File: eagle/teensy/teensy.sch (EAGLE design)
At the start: 5 parts

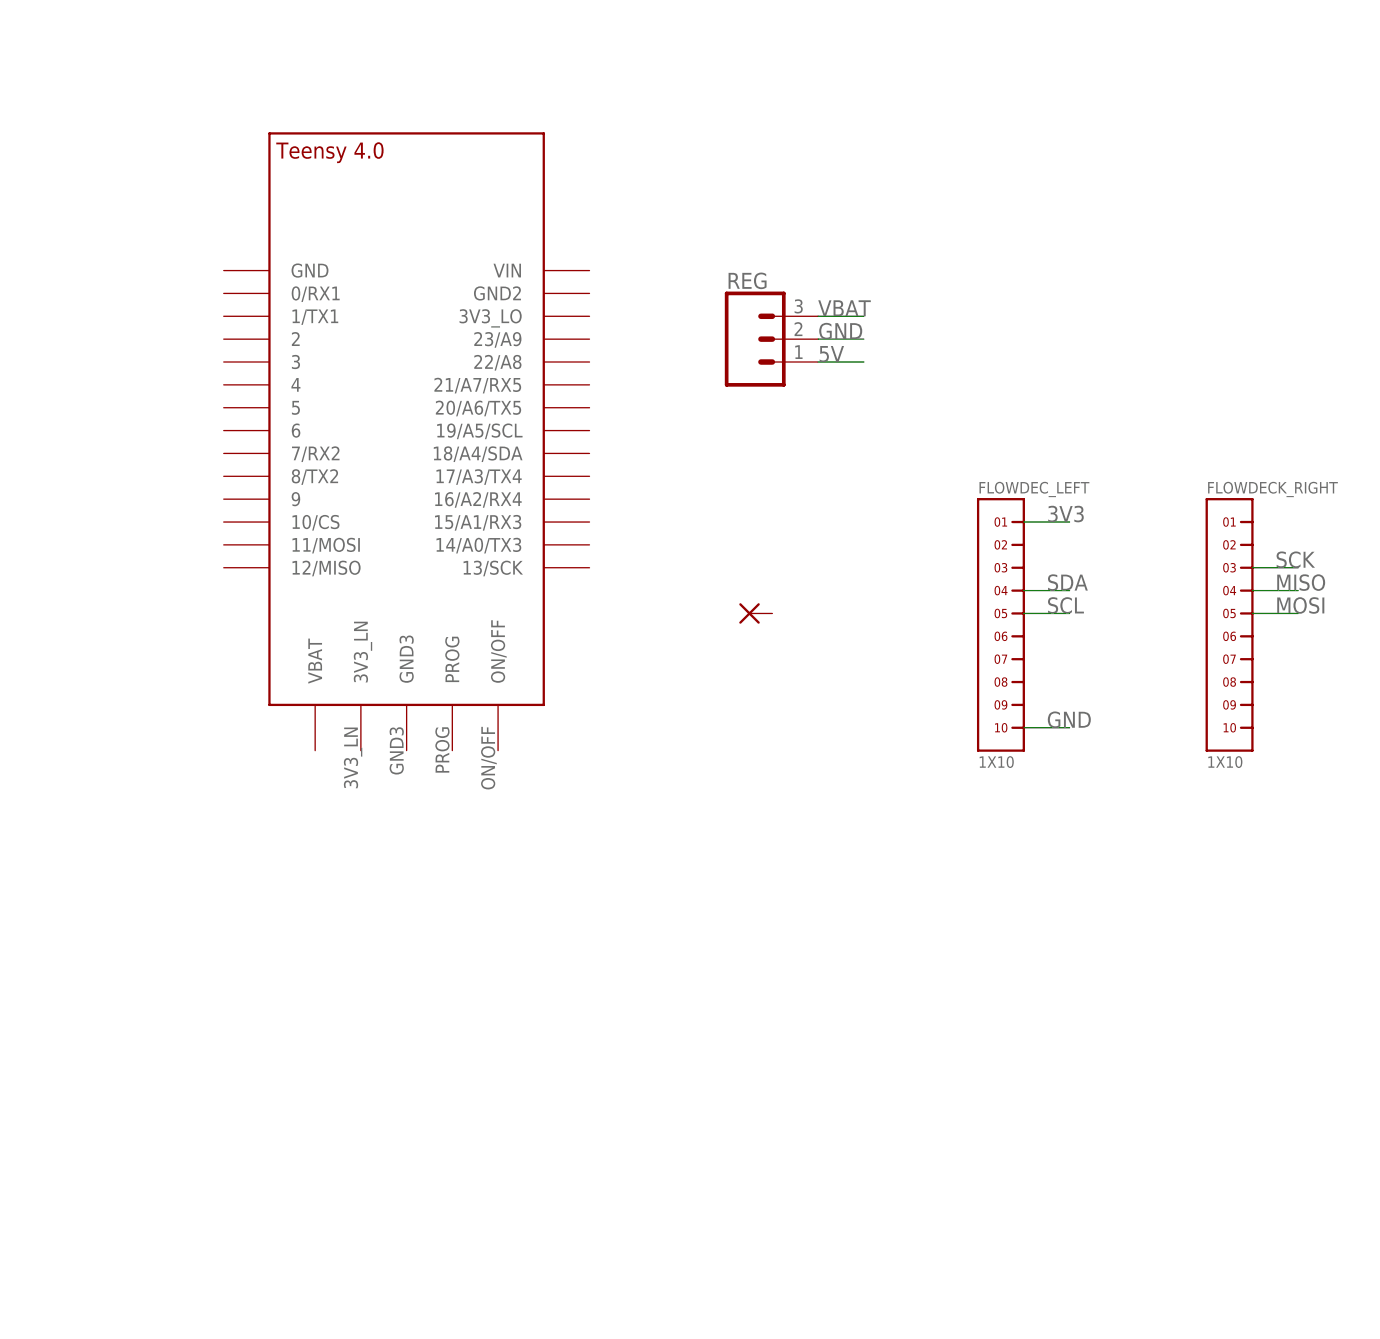
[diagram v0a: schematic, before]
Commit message: renamed:    eagle/teensy/core.sch -> eagle/teensy/teensy.sch
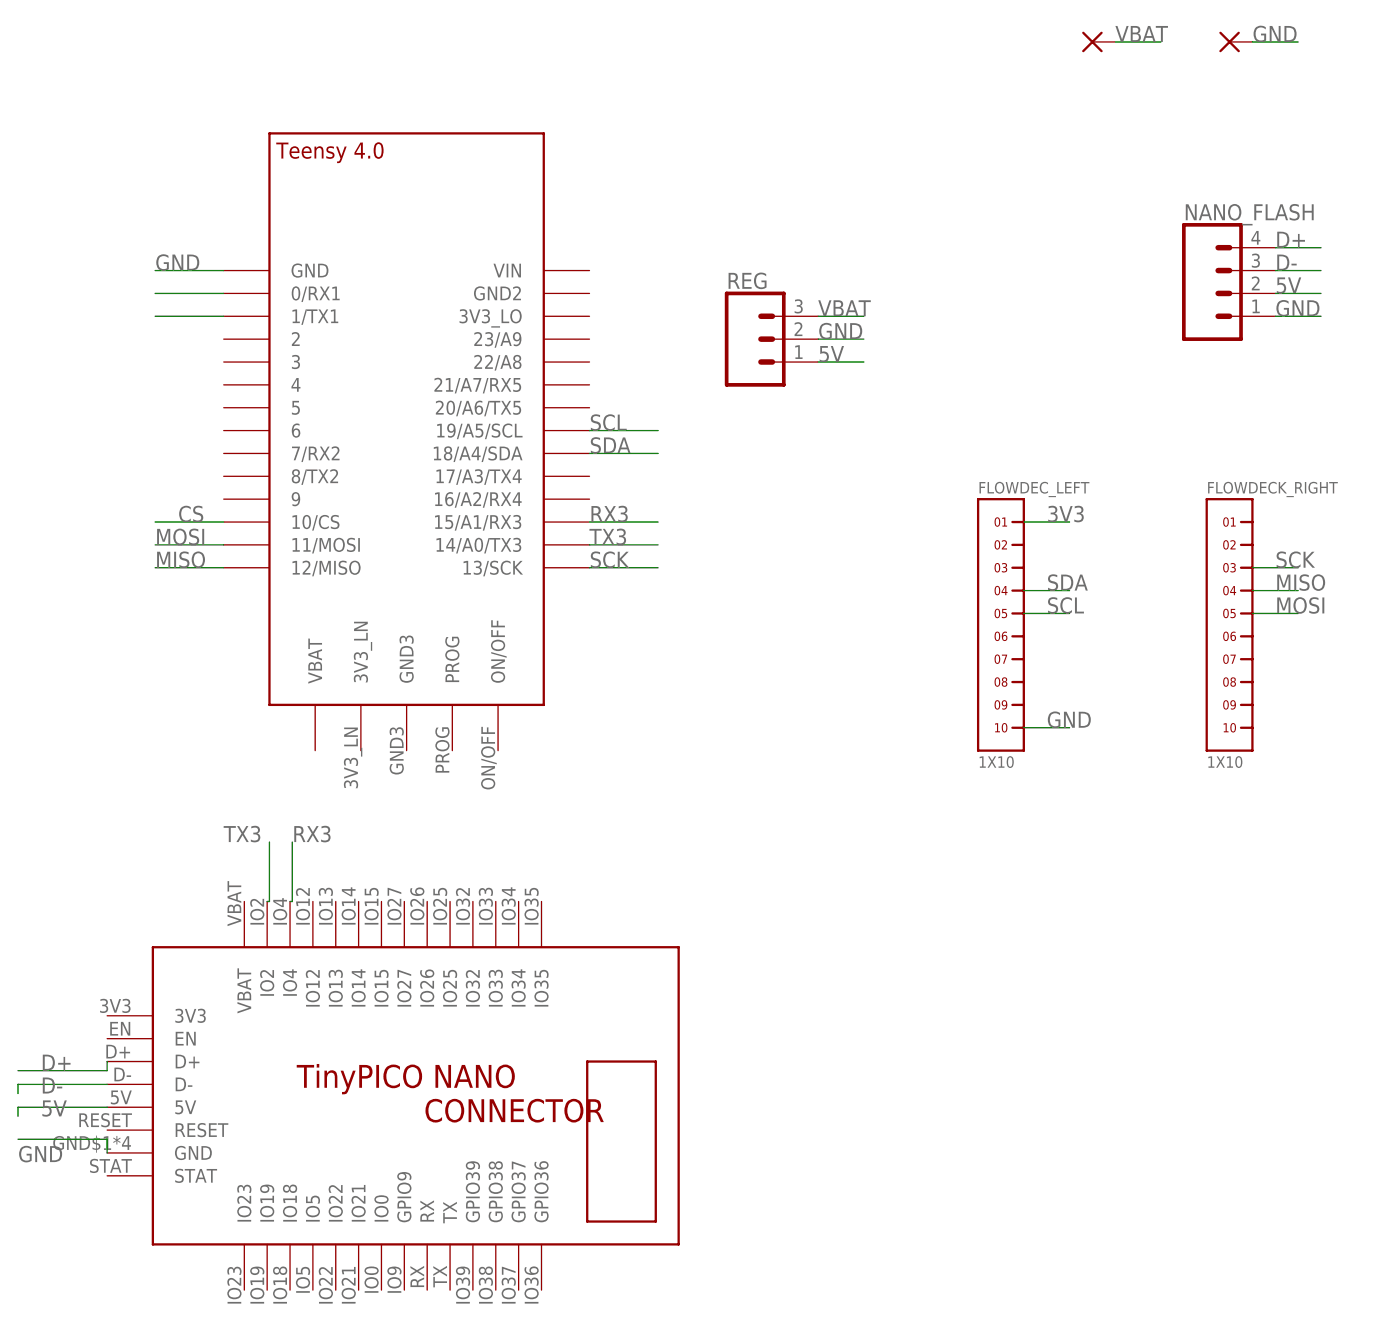
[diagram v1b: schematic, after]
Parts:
- removed PAD18: (no value), wirepad:SMD2
- added GND, VBAT: (no value), wirepad:SMD5
- added NANO_FLASH: (no value), SparkFun-Connectors:CONN_041X04_NO_SILK
- added U$2: TINYPICO-NANO-CONNECTOR, TinyPICO_NANO_Eagle:TINYPICO-NANO-CONNECTOR
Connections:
- new net CS: U$1.10/CS
- new net D+: NANO_FLASH.4, U$2.D+
- new net D-: NANO_FLASH.3, U$2.D-
- new net N$8: U$1.0/RX1
- new net N$9: U$1.1/TX1
- new net RX3: U$1.15/A1/RX3, U$2.IO4
- new net TX3: U$1.14/A0/TX3, U$2.IO2
- net 5V: now also NANO_FLASH.2, U$2.5V
- net GND: now also GND.P, NANO_FLASH.1, U$1.GND, U$2.GND
- net MISO: now also U$1.12/MISO
- net MOSI: now also U$1.11/MOSI
- net SCK: now also U$1.13/SCK
- net SCL: now also U$1.19/A5/SCL
- net SDA: now also U$1.18/A4/SDA
- net VBAT: now also VBAT.P
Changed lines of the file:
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@@
 <?xml version="1.0" encoding="utf-8"?>
 <!DOCTYPE eagle SYSTEM "eagle.dtd">
-<eagle version="9.6.2">
+<eagle version="9.1.1">
 <drawing>
 <settings>
@@
 <parts>
 <part name="REG" library="SparkFun-Connectors" deviceset="CONN_03" device="1X03_NO_SILK"/>
-<part name="PAD18" library="wirepad" deviceset="SMD2" device=""/>
 <part name="U$1" library="TEENSY 4.0" deviceset="TEENSY_4.0" device=""/>
 <part name="FLOWDEC_LEFT" library="headers(2mm)" deviceset="1X10" device=""/>
 <part name="FLOWDECK_RIGHT" library="headers(2mm)" deviceset="1X10" device=""/>
+<part name="U$2" library="TinyPICO_NANO_Eagle" deviceset="TINYPICO-NANO-CONNECTOR" device=""/>
+<part name="VBAT" library="wirepad" deviceset="SMD5" device=""/>
+<part name="GND" library="wirepad" deviceset="SMD5" device=""/>
+<part name="NANO_FLASH" library="SparkFun-Connectors" deviceset="CONN_04" device="1X04_NO_SILK"/>
 </parts>
 <sheets>
@@
 <attribute name="NAME" x="50.8" y="114.808" size="1.778" layer="95" font="vector"/>
 </instance>
-<instance part="PAD18" gate="1" x="53.34" y="78.74" smashed="yes">
-<attribute name="VALUE" x="52.197" y="75.438" size="1.778" layer="96"/>
-</instance>
 <instance part="U$1" gate="G$1" x="15.24" y="104.14" smashed="yes"/>
 <instance part="FLOWDEC_LEFT" gate="G$1" x="81.28" y="76.2" smashed="yes">
@@
 <attribute name="VALUE" x="104.14" y="61.595" size="1.27" layer="96" font="vector"/>
 </instance>
+<instance part="U$2" gate="G$1" x="15.24" y="25.4"/>
+<instance part="VBAT" gate="1" x="91.44" y="142.24" smashed="yes">
+<attribute name="VALUE" x="90.297" y="138.938" size="1.778" layer="96"/>
+</instance>
+<instance part="GND" gate="1" x="106.68" y="142.24" smashed="yes">
+<attribute name="VALUE" x="105.537" y="138.938" size="1.778" layer="96"/>
+</instance>
+<instance part="NANO_FLASH" gate="J1" x="106.68" y="114.3"/>
 </instances>
 <busses>
@@
 <label x="86.36" y="66.04" size="1.778" layer="95"/>
 </segment>
+<segment>
+<pinref part="GND" gate="1" pin="P"/>
+<wire x1="109.22" y1="142.24" x2="114.3" y2="142.24" width="0.1524" layer="91"/>
+<label x="109.22" y="142.24" size="1.778" layer="95"/>
+</segment>
+<segment>
+<pinref part="U$2" gate="G$1" pin="GND"/>
+<wire x1="-18.034" y1="18.796" x2="-18.034" y2="20.32" width="0.1524" layer="91"/>
+<wire x1="-18.034" y1="20.32" x2="-27.94" y2="20.32" width="0.1524" layer="91"/>
+<label x="-27.94" y="17.78" size="1.778" layer="95"/>
+</segment>
+<segment>
+<pinref part="U$1" gate="G$1" pin="GND"/>
+<wire x1="-5.08" y1="116.84" x2="-12.7" y2="116.84" width="0.1524" layer="91"/>
+<label x="-12.7" y="116.84" size="1.778" layer="95"/>
+</segment>
+<segment>
+<pinref part="NANO_FLASH" gate="J1" pin="1"/>
+<wire x1="111.76" y1="111.76" x2="116.84" y2="111.76" width="0.1524" layer="91"/>
+<label x="111.76" y="111.76" size="1.778" layer="95"/>
+</segment>
 </net>
 <net name="5V" class="0">
@@
 <label x="60.96" y="106.68" size="1.778" layer="95"/>
 </segment>
+<segment>
+<pinref part="U$2" gate="G$1" pin="5V"/>
+<wire x1="-18.034" y1="23.876" x2="-27.94" y2="23.876" width="0.1524" layer="91"/>
+<wire x1="-27.94" y1="23.876" x2="-27.94" y2="22.86" width="0.1524" layer="91"/>
+<label x="-25.4" y="22.86" size="1.778" layer="95"/>
+</segment>
+<segment>
+<pinref part="NANO_FLASH" gate="J1" pin="2"/>
+<wire x1="111.76" y1="114.3" x2="116.84" y2="114.3" width="0.1524" layer="91"/>
+<label x="111.76" y="114.3" size="1.778" layer="95"/>
+</segment>
 </net>
 <net name="VBAT" class="0">
@@
 <label x="60.96" y="111.76" size="1.778" layer="95"/>
 </segment>
+<segment>
+<pinref part="VBAT" gate="1" pin="P"/>
+<wire x1="93.98" y1="142.24" x2="99.06" y2="142.24" width="0.1524" layer="91"/>
+<label x="93.98" y="142.24" size="1.778" layer="95"/>
+</segment>
 </net>
 <net name="3V3" class="0">
@@
 <label x="86.36" y="81.28" size="1.778" layer="95"/>
 </segment>
+<segment>
+<pinref part="U$1" gate="G$1" pin="18/A4/SDA"/>
+<wire x1="35.56" y1="96.52" x2="43.18" y2="96.52" width="0.1524" layer="91"/>
+<label x="35.56" y="96.52" size="1.778" layer="95"/>
+</segment>
 </net>
 <net name="SCL" class="0">
@@
 <label x="86.36" y="78.74" size="1.778" layer="95"/>
 </segment>
+<segment>
+<pinref part="U$1" gate="G$1" pin="19/A5/SCL"/>
+<wire x1="35.56" y1="99.06" x2="43.18" y2="99.06" width="0.1524" layer="91"/>
+<label x="35.56" y="99.06" size="1.778" layer="95"/>
+</segment>
 </net>
 <net name="SCK" class="0">
@@
 <label x="111.76" y="83.82" size="1.778" layer="95"/>
 </segment>
+<segment>
+<pinref part="U$1" gate="G$1" pin="13/SCK"/>
+<wire x1="35.56" y1="83.82" x2="43.18" y2="83.82" width="0.1524" layer="91"/>
+<label x="35.56" y="83.82" size="1.778" layer="95"/>
+</segment>
 </net>
 <net name="MISO" class="0">
@@
 <label x="111.76" y="81.28" size="1.778" layer="95"/>
 </segment>
+<segment>
+<pinref part="U$1" gate="G$1" pin="12/MISO"/>
+<wire x1="-5.08" y1="83.82" x2="-12.7" y2="83.82" width="0.1524" layer="91"/>
+<label x="-12.7" y="83.82" size="1.778" layer="95"/>
+</segment>
 </net>
 <net name="MOSI" class="0">
@@
 <label x="111.76" y="78.74" size="1.778" layer="95"/>
 </segment>
-</net>
+<segment>
+<pinref part="U$1" gate="G$1" pin="11/MOSI"/>
+<wire x1="-12.7" y1="86.36" x2="-5.08" y2="86.36" width="0.1524" layer="91"/>
+<label x="-12.7" y="86.36" size="1.778" layer="95"/>
+</segment>
+</net>
+<net name="D+" class="0">
+<segment>
+<pinref part="U$2" gate="G$1" pin="D+"/>
+<wire x1="-18.034" y1="28.956" x2="-18.034" y2="27.94" width="0.1524" layer="91"/>
+<wire x1="-18.034" y1="27.94" x2="-27.94" y2="27.94" width="0.1524" layer="91"/>
+<label x="-25.4" y="27.94" size="1.778" layer="95"/>
+</segment>
+<segment>
+<pinref part="NANO_FLASH" gate="J1" pin="4"/>
+<wire x1="111.76" y1="119.38" x2="116.84" y2="119.38" width="0.1524" layer="91"/>
+<label x="111.76" y="119.38" size="1.778" layer="95"/>
+</segment>
+</net>
+<net name="D-" class="0">
+<segment>
+<pinref part="U$2" gate="G$1" pin="D-"/>
+<wire x1="-18.034" y1="26.416" x2="-27.94" y2="26.416" width="0.1524" layer="91"/>
+<wire x1="-27.94" y1="26.416" x2="-27.94" y2="25.4" width="0.1524" layer="91"/>
+<label x="-25.4" y="25.4" size="1.778" layer="95"/>
+</segment>
+<segment>
+<pinref part="NANO_FLASH" gate="J1" pin="3"/>
+<wire x1="111.76" y1="116.84" x2="116.84" y2="116.84" width="0.1524" layer="91"/>
+<label x="111.76" y="116.84" size="1.778" layer="95"/>
+</segment>
+</net>
+<net name="CS" class="0">
+<segment>
+<pinref part="U$1" gate="G$1" pin="10/CS"/>
+<wire x1="-5.08" y1="88.9" x2="-12.7" y2="88.9" width="0.1524" layer="91"/>
+<label x="-10.16" y="88.9" size="1.778" layer="95"/>
+</segment>
+</net>
+<net name="N$8" class="0">
+<segment>
+<pinref part="U$1" gate="G$1" pin="0/RX1"/>
+<wire x1="-5.08" y1="114.3" x2="-12.7" y2="114.3" width="0.1524" layer="91"/>
+</segment>
+</net>
+<net name="N$9" class="0">
+<segment>
+<pinref part="U$1" gate="G$1" pin="1/TX1"/>
+<wire x1="-5.08" y1="111.76" x2="-12.7" y2="111.76" width="0.1524" layer="91"/>
+</segment>
+</net>
+<net name="TX3" class="0">
+<segment>
+<pinref part="U$1" gate="G$1" pin="14/A0/TX3"/>
+<wire x1="35.56" y1="86.36" x2="43.18" y2="86.36" width="0.1524" layer="91"/>
+<label x="35.56" y="86.36" size="1.778" layer="95"/>
+</segment>
+<segment>
+<pinref part="U$2" gate="G$1" pin="IO2"/>
+<wire x1="-0.254" y1="46.736" x2="0" y2="46.736" width="0.1524" layer="91"/>
+<wire x1="0" y1="46.736" x2="0" y2="53.34" width="0.1524" layer="91"/>
+<label x="-5.08" y="53.34" size="1.778" layer="95"/>
+</segment>
+</net>
+<net name="RX3" class="0">
+<segment>
+<pinref part="U$1" gate="G$1" pin="15/A1/RX3"/>
+<wire x1="35.56" y1="88.9" x2="43.18" y2="88.9" width="0.1524" layer="91"/>
+<label x="35.56" y="88.9" size="1.778" layer="95"/>
+</segment>
+<segment>
+<pinref part="U$2" gate="G$1" pin="IO4"/>
+<wire x1="2.286" y1="46.736" x2="2.54" y2="46.736" width="0.1524" layer="91"/>
+<wire x1="2.54" y1="46.736" x2="2.54" y2="53.34" width="0.1524" layer="91"/>
+<label x="2.54" y="53.34" size="1.778" layer="95"/>
+</segment>
+</net>
